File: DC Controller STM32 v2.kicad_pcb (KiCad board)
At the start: 4 copper layers, 154 x 154 mm, 297 parts, among them J1 SM08B-CPTK-1A-TBL, J10 Conn_01x04, J11 Conn_02x06_Odd_Even, J12 Conn_01x03, J13 Conn_01x02, J14 Conn_02x05_Odd_Even, J15 Conn_01x06, J16 TC2030-MCP, J17 Conn_01x04, J18 TC2030-MCP, J19 Conn_01x02, J2 Conn_02x20_Odd_Even, J3 SM02B-CPTK-1A-TB, J4 Conn_01x04, J5 BM02B-CPTK-1A-TB, J6 BM50B-SHLDS-G-TFT, J7 SM08B-CPTK-1A-TB, J8 BM08B-CPTK-1A-TB, J9 Conn_02x05_Odd_Even, Q1 NCV8402A, Q10 MMBT3904, Q11 MMBT3904, Q12 MMBT3904, Q13 MMBT3904, Q14 MMBT3904, Q15 MMBT3904, Q16 MMBT3904, Q17 MMBT3904, Q18 MMBT3904, Q19 MMBT3904, Q2 MMBT3904, Q20 MMBT3904, Q21 MMBT3904, Q22 MMBT3904, Q23 MMBT3904, Q24 MMBT3904, Q25 MMBT3904, Q3 S8050, Q4 S8050, Q5 NCV8402A, Q6 NCV8402A, Q7 NCV8402A, Q8 NCV8402A, Q9 NCV8402A, SW1 SW_Push, U1 MCP6561x-LT, U10 SGM3204, U11 MP2359, U12 XC6206P332MR, U13 MC34063ABD-TR, U14 TX4314, U15 MAX889RESA+, U2 74LVC1G3157GW, U3 STM32F103RBT6, U4 SN65HVD230, U5 74LVC1G3157GW, U6 MCP2515-I/SO, U7 LTC6992CS6-1, U8 TJA1050T, U9 ATmega328P-AU, Y1 16MHz, Y2 8M0, Y3 16MHz

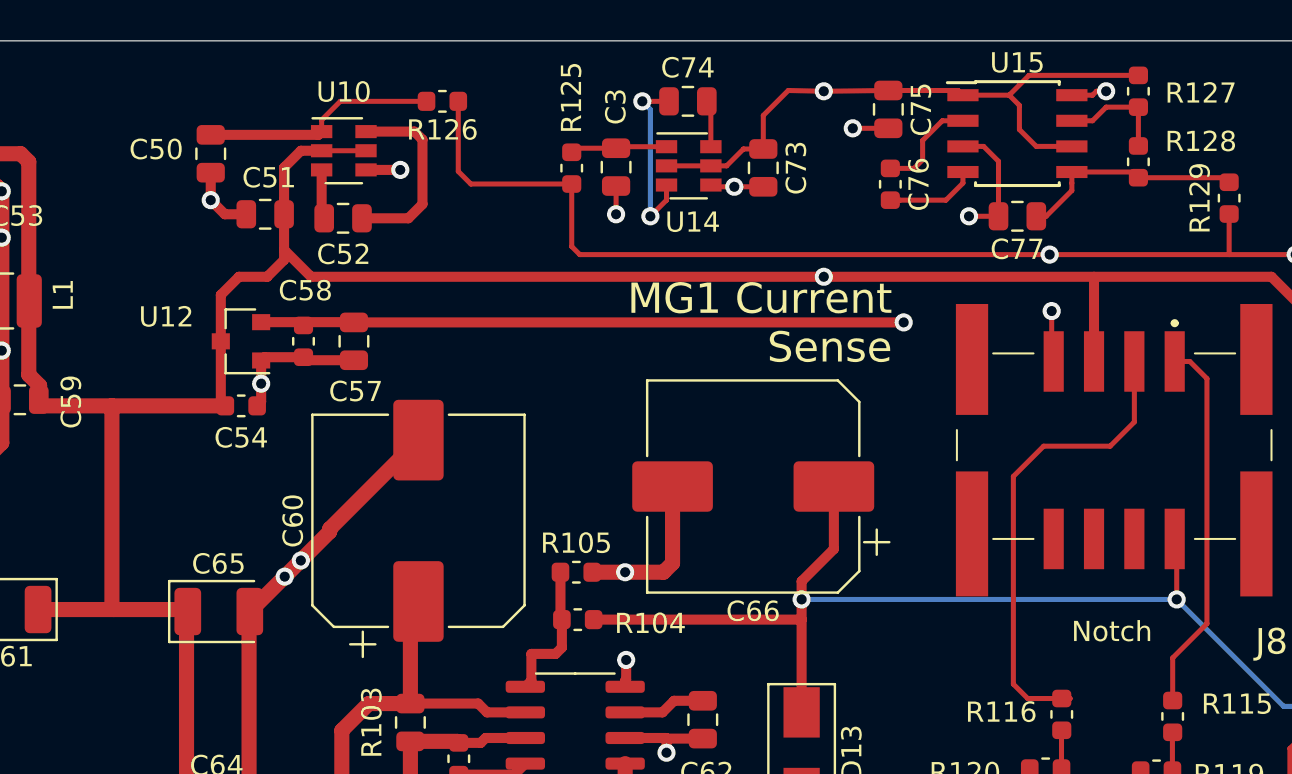
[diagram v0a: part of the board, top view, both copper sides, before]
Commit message: removed SG3204 and TX4313 -5V charge pumps and added LM2776 in their place
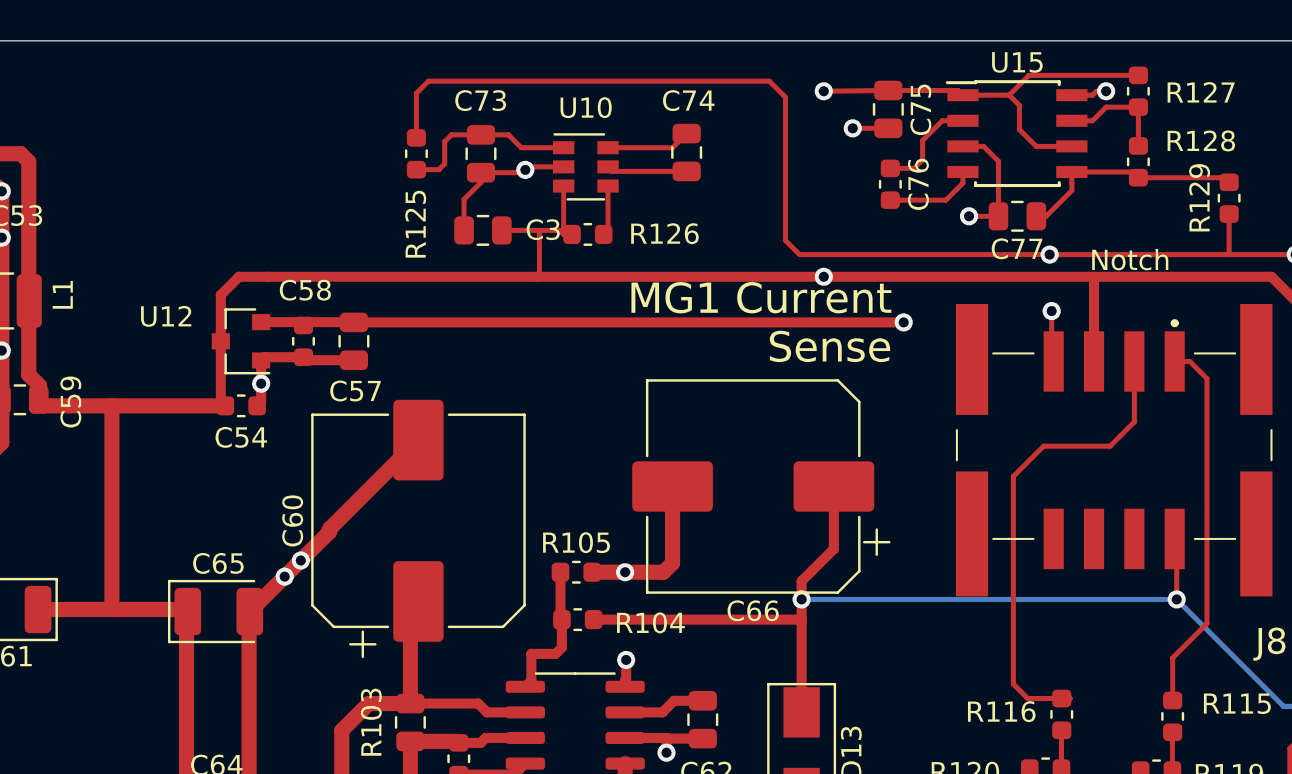
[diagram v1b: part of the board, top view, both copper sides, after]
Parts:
- removed C50, C51, C52: 4.7uF, Capacitor_SMD:C_0805_2012Metric
- removed U14: TX4314, Package_TO_SOT_SMD:SOT-23-6
- C74: value 4.7uF -> 1uF
- R126: value 0R -> 1k
- R127, R128: value 56k -> NF 56k
- R129: value 0R -> NF
- U10: value SGM3204 -> LM2776
- moved C73 14.0 mm to (69.4, -148.4)
- moved U10 12.0 mm to (74.6, -147.8)
- moved R126 9.78 mm to (74.7, -144.4), turned to 0 degrees
- moved R125 7.73 mm to (66.2, -148.4), turned to 270 degrees
- moved C3 7.31 mm to (69.5, -144.6), turned to 180 degrees
- moved C74 2.54 mm to (79.6, -148.5), turned to 90 degrees
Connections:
- C3 pad 1: Net-(C3-Pad1) -> +5V
- C73 pad 1: +5V -> Net-(C73-Pad1)
- R125 pad 2: Net-(C3-Pad1) -> Net-(C73-Pad1)
- R126 pad 1: -5V -> +5V
- R126 pad 2: Net-(C50-Pad1) -> Net-(R126-Pad2)
- U10 pad 1: Net-(C50-Pad1) -> Net-(C73-Pad1)
- U10 pad 2: +5V -> GND
- U10 pad 3: Net-(C52-Pad1) -> +5V
- U10 pad 4: GND -> Net-(R126-Pad2)
- U10 pad 5: +5V -> Net-(C74-Pad1)
- U10 pad 6: Net-(C52-Pad2) -> Net-(C74-Pad2)
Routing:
- net +5V: track 831.0 -> 818.7 mm
- net Net-(C50-Pad1): track 11.5 -> 0.00 mm
- net Net-(C52-Pad2): track 9.46 -> 0.00 mm
- net Net-(C73-Pad1): track 0.00 -> 8.92 mm
- net -5V: track 166.9 -> 172.1 mm
- net Net-(C74-Pad1): track 9.07 -> 3.99 mm, vias 2 -> 0
- net Net-(C3-Pad1): track 4.81 -> 0.00 mm
- net Net-(R126-Pad2): track 0.00 -> 2.49 mm
- net Net-(C52-Pad1): track 2.45 -> 0.00 mm
- net Net-(C74-Pad2): track 2.33 -> 4.19 mm
- net GND: track 432.2 -> 430.5 mm, vias 107 -> 104
